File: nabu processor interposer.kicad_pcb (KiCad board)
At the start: 2 copper layers, 54 parts, among them IC1 Aries 40-600-21, IC2 Z80CPU-DIP-SOCKET, IC3 CTC-QFP-44, IC4 CTC-QFP-44, IC5 DMA-PLCC-44-CMOS, IC6 DMA-PLCC-44-CMOS, IC7 DMA-PLCC-44-CMOS, IC8 DMA-PLCC-44-CMOS, J1 5V EXTRA, J2 WRITE PROTECT, J3 AVR-JTAG-10, U1 LP3963-3.3, U10 SST39SF040, U11 SST39SF040, U12 SST39SF040, U13 74AHC139, U14 74HC245, U15 74HC245, U16 74HC245, U17 74HC245, U18 ATF1508-100, U2 TXB0108DQSR, U3 TXB0108DQSR, U4 TXB0108DQSR, U5 74LVC1G04, U6 TXB0108DQSR, U7 AS6C1616, U8 TXB0108DQSR, U9 SST39SF040

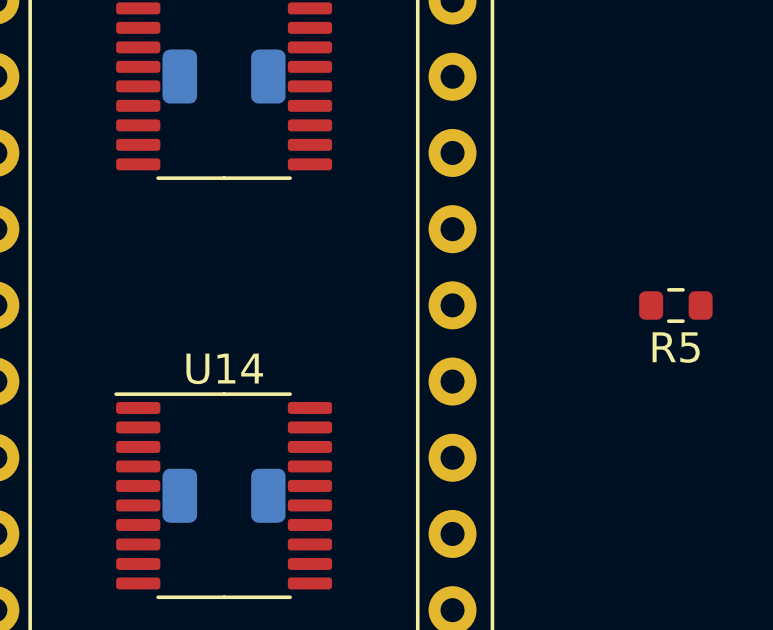
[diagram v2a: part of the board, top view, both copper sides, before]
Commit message: simplified the vhdl code for the mapper by removing some of the more complex initilization logic used:     flags was initially intended to be used for reset logic but     was determined to be un-needed if we initialise as done in     the generate loop for the bank registers
    control_regs was going to shadow the main system control
    register, but only contain the bits not used by the system.
    removed for now since im not sure that those bits arent
    written anyway by software. the eventual intention is to
    allow bits 7 and 8 to determine if mapping is wanted at all
    and to boot from interposer rom instead of network (which may
    end up being done anyway if i can figure out how)

    other logical simplfications where also performed such as
    removing the need for plumbing the address bus through the
    glue logic at all. this is reflected in the schematics

    the interposer glue logic now only needs 8 address lines
    to swing the extended address bus around.
the schematics where simplified so that the entire address bus
isnt routed through the interposer now. may end up using a
smaller 1508 beucase of this.

a liscense file was added to the vhd file(s) and the mapper file
was broken up into a package and main buildable, the beginings of
a test bench was added, now begins the slog of verification!
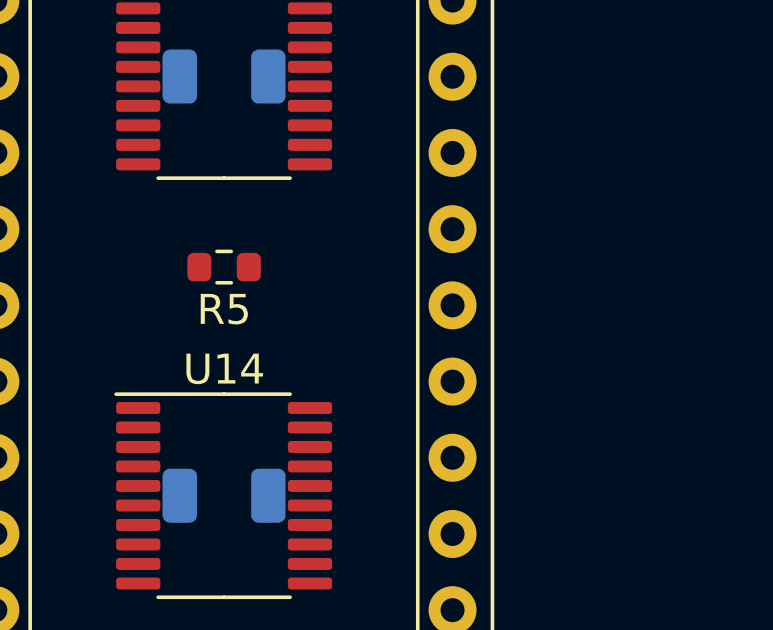
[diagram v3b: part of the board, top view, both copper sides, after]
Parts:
- moved R5 15.1 mm to (217.2, 99.1)
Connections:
- U10 pad 10: /GLUE/EAB2 -> /BRAINS/AB2
- U10 pad 11: /GLUE/EAB1 -> /BRAINS/AB1
- U10 pad 12: /GLUE/EAB0 -> /BRAINS/AB0
- U10 pad 23: /GLUE/EAB10 -> /BRAINS/AB10
- U10 pad 25: /GLUE/EAB11 -> /BRAINS/AB11
- U10 pad 26: /GLUE/EAB9 -> /BRAINS/AB9
- U10 pad 27: /GLUE/EAB8 -> /BRAINS/AB8
- U10 pad 28: /GLUE/EAB13 -> /BRAINS/AB13
- U10 pad 4: /GLUE/EAB12 -> /BRAINS/AB12
- U10 pad 5: /GLUE/EAB7 -> /BRAINS/AB7
- U10 pad 6: /GLUE/EAB6 -> /BRAINS/AB6
- U10 pad 7: /GLUE/EAB5 -> /BRAINS/AB5
- U10 pad 8: /GLUE/EAB4 -> /BRAINS/AB4
- U10 pad 9: /GLUE/EAB3 -> /BRAINS/AB3
- U11 pad 10: /GLUE/EAB2 -> /BRAINS/AB2
- U11 pad 11: /GLUE/EAB1 -> /BRAINS/AB1
- U11 pad 12: /GLUE/EAB0 -> /BRAINS/AB0
- U11 pad 23: /GLUE/EAB10 -> /BRAINS/AB10
- U11 pad 25: /GLUE/EAB11 -> /BRAINS/AB11
- U11 pad 26: /GLUE/EAB9 -> /BRAINS/AB9
- U11 pad 27: /GLUE/EAB8 -> /BRAINS/AB8
- U11 pad 28: /GLUE/EAB13 -> /BRAINS/AB13
- U11 pad 4: /GLUE/EAB12 -> /BRAINS/AB12
- U11 pad 5: /GLUE/EAB7 -> /BRAINS/AB7
- U11 pad 6: /GLUE/EAB6 -> /BRAINS/AB6
- U11 pad 7: /GLUE/EAB5 -> /BRAINS/AB5
- U11 pad 8: /GLUE/EAB4 -> /BRAINS/AB4
- U11 pad 9: /GLUE/EAB3 -> /BRAINS/AB3
- U12 pad 10: /GLUE/EAB2 -> /BRAINS/AB2
- U12 pad 11: /GLUE/EAB1 -> /BRAINS/AB1
- U12 pad 12: /GLUE/EAB0 -> /BRAINS/AB0
- U12 pad 23: /GLUE/EAB10 -> /BRAINS/AB10
- U12 pad 25: /GLUE/EAB11 -> /BRAINS/AB11
- U12 pad 26: /GLUE/EAB9 -> /BRAINS/AB9
- U12 pad 27: /GLUE/EAB8 -> /BRAINS/AB8
- U12 pad 28: /GLUE/EAB13 -> /BRAINS/AB13
- U12 pad 4: /GLUE/EAB12 -> /BRAINS/AB12
- U12 pad 5: /GLUE/EAB7 -> /BRAINS/AB7
- U12 pad 6: /GLUE/EAB6 -> /BRAINS/AB6
- U12 pad 7: /GLUE/EAB5 -> /BRAINS/AB5
- U12 pad 8: /GLUE/EAB4 -> /BRAINS/AB4
- U12 pad 9: /GLUE/EAB3 -> /BRAINS/AB3
- U18 pad 27: /BRAINS/AB0 -> unconnected-(U18-Pad27)
- U18 pad 28: /BRAINS/AB1 -> unconnected-(U18-Pad28)
- U18 pad 29: /BRAINS/AB2 -> unconnected-(U18-Pad29)
- U18 pad 30: /BRAINS/AB3 -> unconnected-(U18-Pad30)
- U18 pad 31: /BRAINS/AB4 -> unconnected-(U18-Pad31)
- U18 pad 32: /BRAINS/AB5 -> unconnected-(U18-Pad32)
- U18 pad 33: /BRAINS/AB6 -> unconnected-(U18-Pad33)
- U18 pad 35: /BRAINS/AB7 -> unconnected-(U18-Pad35)
- U18 pad 36: /BRAINS/AB8 -> unconnected-(U18-Pad36)
- U18 pad 37: /BRAINS/AB9 -> unconnected-(U18-Pad37)
- U18 pad 40: /BRAINS/AB10 -> unconnected-(U18-Pad40)
- U18 pad 42: /BRAINS/AB11 -> unconnected-(U18-Pad42)
- U18 pad 44: /BRAINS/AB12 -> unconnected-(U18-Pad44)
- U18 pad 45: /BRAINS/AB13 -> unconnected-(U18-Pad45)
- U18 pad 46: /BRAINS/AB14 -> unconnected-(U18-Pad46)
- U18 pad 47: /BRAINS/AB15 -> unconnected-(U18-Pad47)
- U18 pad 52: unconnected-(U18-Pad52) -> /BRAINS/AB2
- U18 pad 53: unconnected-(U18-Pad53) -> /BRAINS/AB3
- U18 pad 54: unconnected-(U18-Pad54) -> /BRAINS/AB4
- U18 pad 55: unconnected-(U18-Pad55) -> /BRAINS/AB5
- U18 pad 56: unconnected-(U18-Pad56) -> /BRAINS/AB6
- U18 pad 57: /GLUE/EAB0 -> /BRAINS/AB7
- U18 pad 58: /GLUE/EAB1 -> /BRAINS/AB14
- U18 pad 60: /GLUE/EAB2 -> /BRAINS/AB15
- U18 pad 61: /GLUE/EAB3 -> unconnected-(U18-Pad61)
- U18 pad 63: /GLUE/EAB4 -> unconnected-(U18-Pad63)
- U18 pad 64: /GLUE/EAB5 -> unconnected-(U18-Pad64)
- U18 pad 65: /GLUE/EAB6 -> unconnected-(U18-Pad65)
- U18 pad 67: /GLUE/EAB7 -> unconnected-(U18-Pad67)
- U18 pad 68: /GLUE/EAB8 -> unconnected-(U18-Pad68)
- U18 pad 69: /GLUE/EAB9 -> unconnected-(U18-Pad69)
- U18 pad 70: /GLUE/EAB10 -> unconnected-(U18-Pad70)
- U18 pad 71: /GLUE/EAB11 -> unconnected-(U18-Pad71)
- U18 pad 72: /GLUE/EAB12 -> unconnected-(U18-Pad72)
- U18 pad 75: /GLUE/EAB13 -> unconnected-(U18-Pad75)
- U3 pad 11: /GLUE/EAB7 -> /BRAINS/AB7
- U3 pad 12: /GLUE/EAB6 -> /BRAINS/AB6
- U3 pad 13: /GLUE/EAB5 -> /BRAINS/AB5
- U3 pad 14: /GLUE/EAB4 -> /BRAINS/AB4
- U3 pad 17: /GLUE/EAB3 -> /BRAINS/AB3
- U3 pad 18: /GLUE/EAB2 -> /BRAINS/AB2
- U3 pad 19: /GLUE/EAB1 -> /BRAINS/AB1
- U3 pad 20: /GLUE/EAB0 -> /BRAINS/AB0
- U4 pad 13: /GLUE/EAB13 -> /BRAINS/AB13
- U4 pad 14: /GLUE/EAB12 -> /BRAINS/AB12
- U4 pad 17: /GLUE/EAB11 -> /BRAINS/AB11
- U4 pad 18: /GLUE/EAB10 -> /BRAINS/AB10
- U4 pad 19: /GLUE/EAB9 -> /BRAINS/AB9
- U4 pad 20: /GLUE/EAB8 -> /BRAINS/AB8
- U9 pad 10: /GLUE/EAB2 -> /BRAINS/AB2
- U9 pad 11: /GLUE/EAB1 -> /BRAINS/AB1
- U9 pad 12: /GLUE/EAB0 -> /BRAINS/AB0
- U9 pad 23: /GLUE/EAB10 -> /BRAINS/AB10
- U9 pad 25: /GLUE/EAB11 -> /BRAINS/AB11
- U9 pad 26: /GLUE/EAB9 -> /BRAINS/AB9
- U9 pad 27: /GLUE/EAB8 -> /BRAINS/AB8
- U9 pad 28: /GLUE/EAB13 -> /BRAINS/AB13
- U9 pad 4: /GLUE/EAB12 -> /BRAINS/AB12
- U9 pad 5: /GLUE/EAB7 -> /BRAINS/AB7
- U9 pad 6: /GLUE/EAB6 -> /BRAINS/AB6
- U9 pad 7: /GLUE/EAB5 -> /BRAINS/AB5
- U9 pad 8: /GLUE/EAB4 -> /BRAINS/AB4
- U9 pad 9: /GLUE/EAB3 -> /BRAINS/AB3

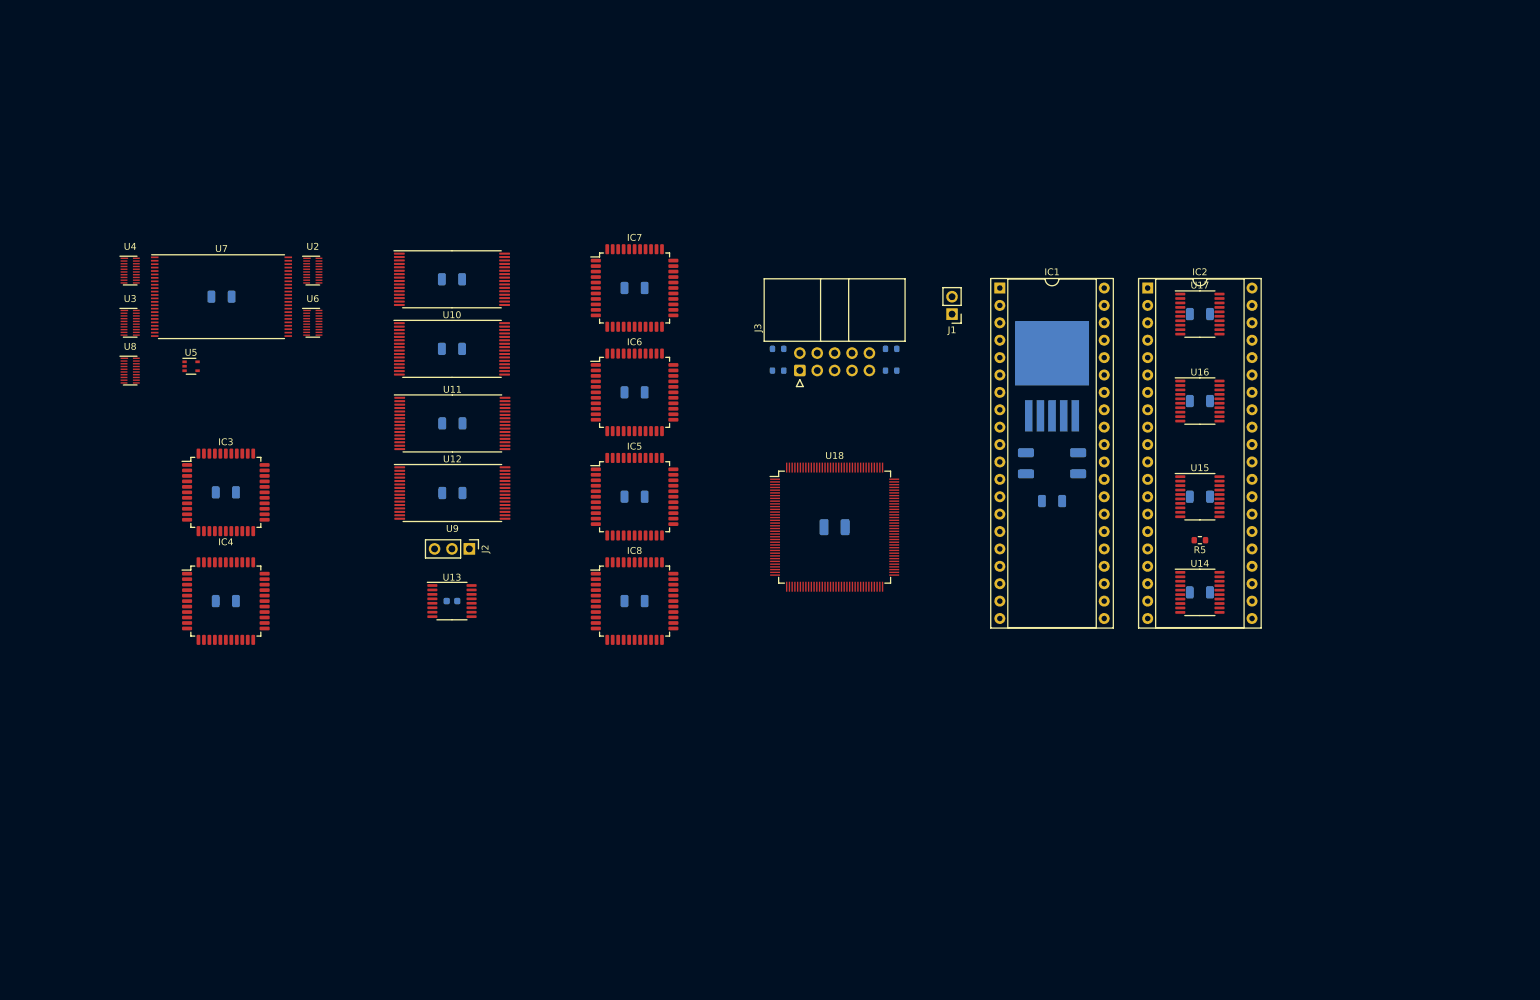
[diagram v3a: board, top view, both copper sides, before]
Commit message: final hardware revision
final update to the hardware:
- removed flash
- added battery backup switch-over
- increased ram to 4MB
- added ramboot/netboot option by using reads to write-only ports to trigger/toggle
- fixed a logic bug i should have caught in writes to the mapper registers (using bits 14&15 instead of 1&0)
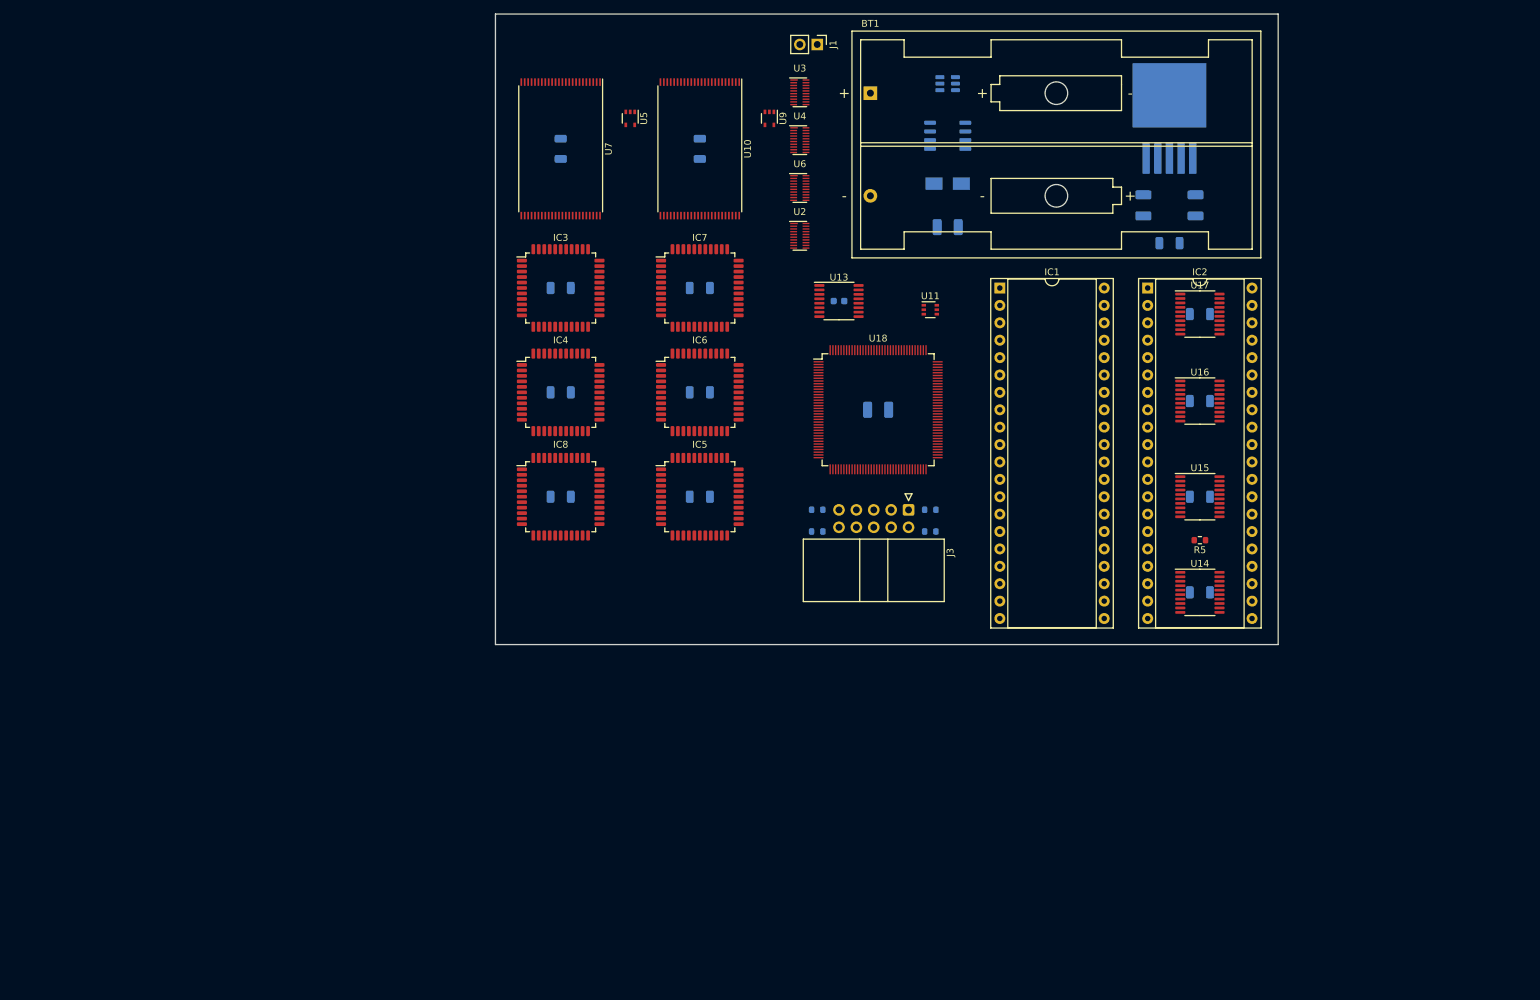
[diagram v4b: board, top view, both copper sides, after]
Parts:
- removed C6, C7: 1U, Capacitor_SMD:C_1206_3216Metric
- removed J2: WRITE PROTECT, Connector_PinHeader_2.54mm:PinHeader_1x03_P2.54mm_Vertical
- removed U12: SST39SF040, Package_SO:TSOP-I-32_14.4x8mm_P0.5mm
- added BT1: Battery, Battery:BatteryHolder_Keystone_2462_2xAA, F.Cu at (169.1, 33.8)
- added D1: B120-E3, Diode_SMD:D_SMA, B.Cu at (180.3, 47.0)
- added Q1: Si4421DY, Package_SO:SO-8_3.9x4.9mm_P1.27mm, B.Cu at (180.3, 40.0)
- C5: value 1U -> 100U TANT; footprint Capacitor_SMD:C_1206_3216Metric -> Capacitor_Tantalum_SMD:CP_EIA-3528-15_AVX-H
- U10: value SST39SF040 -> AS6C1616; footprint Package_SO:TSOP-I-32_14.4x8mm_P0.5mm -> Package_SO:TSOP-I-48_18.4x12mm_P0.5mm
- U11: value SST39SF040 -> 74LVC2G74; footprint Package_SO:TSOP-I-32_14.4x8mm_P0.5mm -> Package_TO_SOT_SMD:SOT-363_SC-70-6
- U8: value TXB0108DQSR -> LTC4412xS6; footprint Package_SON:USON-20_2x4mm_P0.4mm -> Package_TO_SOT_SMD:TSOT-23-6; moved to B.Cu
- U9: value SST39SF040 -> 74LVC1G04; footprint Package_SO:TSOP-I-32_14.4x8mm_P0.5mm -> Package_TO_SOT_SMD:SOT-353_SC-70-5
- moved U8 126.5 mm to (180.3, 32.4)
- moved U3 103.4 mm to (158.8, 33.7)
- moved U4 99.6 mm to (158.8, 40.6)
- moved C5 74.5 mm to (180.3, 53.3), turned to 0 degrees
- moved U6 73.8 mm to (158.8, 47.6)
- moved U5 73.6 mm to (134.0, 37.5), turned to -90 degrees
- moved U11 71.7 mm to (177.8, 65.4)
- moved C8 71.5 mm to (164.5, 64.1)
- moved U13 71.5 mm to (164.5, 64.1)
- moved U2 71.3 mm to (158.8, 54.6)
- moved C15 57.6 mm to (123.8, 77.5)
- moved IC4 57.6 mm to (123.8, 77.5)
- moved C14 57.3 mm to (123.8, 62.2)
- moved IC3 57.3 mm to (123.8, 62.2)
- moved C3 54.0 mm to (123.8, 41.9), turned to 90 degrees
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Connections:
- C2 pad 1: +3V3 -> Net-(C2-Pad1)
- C5 pad 1: +5V -> +3V3
- U1 pad 4: +3V3 -> Net-(C2-Pad1)
- U10 pad 1: /GLUE/EAB18 -> /RAM/RAB16
- U10 pad 10: /BRAINS/AB2 -> unconnected-(U10-Pad10)
- U10 pad 11: /BRAINS/AB1 -> /RAM/~{RAMWR}
- U10 pad 12: /BRAINS/AB0 -> /RAM/RAB21
- U10 pad 13: /BRAINS/DB0 -> unconnected-(U10-Pad13)
- U10 pad 14: /BRAINS/DB1 -> Net-(U10-Pad14)
- U10 pad 15: /BRAINS/DB2 -> /RAM/RAB0
- U10 pad 16: GND -> /RAM/RAB19
- U10 pad 17: /BRAINS/DB3 -> /RAM/RAB18
- U10 pad 18: /BRAINS/DB4 -> /RAM/RAB8
- U10 pad 19: /BRAINS/DB5 -> /RAM/RAB7
- U10 pad 2: /GLUE/EAB16 -> /RAM/RAB15
- U10 pad 20: /BRAINS/DB6 -> /RAM/RAB6
- U10 pad 21: /BRAINS/DB7 -> /RAM/RAB5
- U10 pad 22: /ROM/~{ROM_{1}} -> /RAM/RAB4
- U10 pad 23: /BRAINS/AB10 -> /RAM/RAB3
- U10 pad 24: /RAM/~{RD} -> /RAM/RAB2
- U10 pad 25: /BRAINS/AB11 -> /RAM/RAB1
- U10 pad 26: /BRAINS/AB9 -> GND
- U10 pad 27: /BRAINS/AB8 -> GND
- U10 pad 28: /BRAINS/AB13 -> /RAM/~{RAMRD}
- U10 pad 29: /GLUE/EAB14 -> /RAM/RDB7
- U10 pad 3: /GLUE/EAB15 -> /RAM/RAB14
- U10 pad 30: /GLUE/EAB17 -> /RAM/RDB7
- U10 pad 31: /ROM/~{WRPR} -> /RAM/RDB6
- U10 pad 32: +5V -> /RAM/RDB6
- U10 pad 4: /BRAINS/AB12 -> /RAM/RAB13
- U10 pad 5: /BRAINS/AB7 -> /RAM/RAB12
- U10 pad 6: /BRAINS/AB6 -> /RAM/RAB11
- U10 pad 7: /BRAINS/AB5 -> /RAM/RAB10
- U10 pad 8: /BRAINS/AB4 -> /RAM/RAB9
- U10 pad 9: /BRAINS/AB3 -> /RAM/RAB20
- U11 pad 1: /GLUE/EAB18 -> GND
- U11 pad 2: /GLUE/EAB16 -> GND
- U11 pad 3: /GLUE/EAB15 -> unconnected-(U11-Pad3)
- U11 pad 4: /BRAINS/AB12 -> GND
- U11 pad 5: /BRAINS/AB7 -> /GLUE/BOOTTYPE
- U11 pad 6: /BRAINS/AB6 -> /GLUE/~{RAMBOOT}
- U13 pad 1: /GLUE/~{ROM} -> /DMA/~{DMA}
- U13 pad 10: /DMA/~{DMASEL_{2}} -> unconnected-(U13-Pad10)
- U13 pad 11: /DMA/~{DMASEL_{1}} -> unconnected-(U13-Pad11)
- U13 pad 12: /DMA/~{DMASEL_{0}} -> unconnected-(U13-Pad12)
- U13 pad 13: /BRAINS/AB1 -> GND
- U13 pad 14: /BRAINS/AB0 -> GND
- U13 pad 15: /DMA/~{DMA} -> +5V
- U13 pad 2: /GLUE/EAB20 -> /BRAINS/AB0
- U13 pad 3: /GLUE/EAB19 -> /BRAINS/AB1
- U13 pad 4: /ROM/~{ROM0} -> /DMA/~{DMASEL_{0}}
- U13 pad 5: /ROM/~{ROM_{1}} -> /DMA/~{DMASEL_{1}}
- U13 pad 6: /ROM/~{ROM_{2}} -> /DMA/~{DMASEL_{2}}
- U13 pad 7: /ROM/~{ROM_{3}} -> /DMA/~{DMASEL_{3}}
- U13 pad 9: /DMA/~{DMASEL_{3}} -> unconnected-(U13-Pad9)
- U18 pad 52: /BRAINS/AB2 -> /BRAINS/AB0
- U18 pad 53: /BRAINS/AB3 -> /BRAINS/AB1
- U18 pad 54: /BRAINS/AB4 -> /BRAINS/AB2
- U18 pad 55: /BRAINS/AB5 -> /BRAINS/AB3
- U18 pad 56: /BRAINS/AB6 -> /BRAINS/AB4
- U18 pad 57: /BRAINS/AB7 -> /BRAINS/AB5
- U18 pad 58: /BRAINS/AB14 -> /BRAINS/AB6
- U18 pad 60: /BRAINS/AB15 -> /BRAINS/AB7
- U18 pad 61: unconnected-(U18-Pad61) -> /BRAINS/AB14
- U18 pad 63: unconnected-(U18-Pad63) -> /BRAINS/AB15
- U18 pad 80: /GLUE/~{ROM} -> /BRAINS/~{SYS}
- U18 pad 81: /BRAINS/~{SYS} -> /BRAINS/DIR
- U18 pad 83: /BRAINS/DIR -> /GLUE/~{NETBOOT}
- U18 pad 84: unconnected-(U18-Pad84) -> /GLUE/~{RAMBOOT}
- U18 pad 92: unconnected-(U18-Pad92) -> /GLUE/BOOTTYPE
- U6 pad 10: GND -> /RAM/~{RAMRD}
- U6 pad 11: GND -> /BRAINS/~{RD}
- U6 pad 12: GND -> /BRAINS/~{WR}
- U6 pad 13: GND -> /GLUE/EAB21
- U6 pad 8: GND -> /RAM/RAB21
- U6 pad 9: GND -> /RAM/~{RAMWR}
- U7 pad 11: Net-(U7-Pad11) -> /RAM/~{RAMWR}
- U7 pad 26: Net-(U7-Pad26) -> /RAM/RAB21
- U7 pad 28: Net-(U7-Pad28) -> /RAM/~{RAMRD}
- U8 pad 1: Net-(U7-Pad28) -> Net-(BT1-Pad1)
- U8 pad 2: Net-(U7-Pad11) -> GND
- U8 pad 3: Net-(U7-Pad26) -> GND
- U8 pad 4: GND -> unconnected-(U8-Pad4)
- U8 pad 5: +3V3 -> Net-(Q1-Pad4)
- U8 pad 6: +3V3 -> Net-(C2-Pad1)
- U9 pad 1: /GLUE/EAB18 -> (no net)
- U9 pad 2: /GLUE/EAB16 -> /RAM/RAB0
- U9 pad 3: /GLUE/EAB15 -> GND
- U9 pad 4: /BRAINS/AB12 -> Net-(U10-Pad14)
- U9 pad 5: /BRAINS/AB7 -> +3V3
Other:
- board outline added: 114.3 x 92.1 mm
- copper layers 2 -> 4
